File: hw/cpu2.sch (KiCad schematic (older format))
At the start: 0 parts

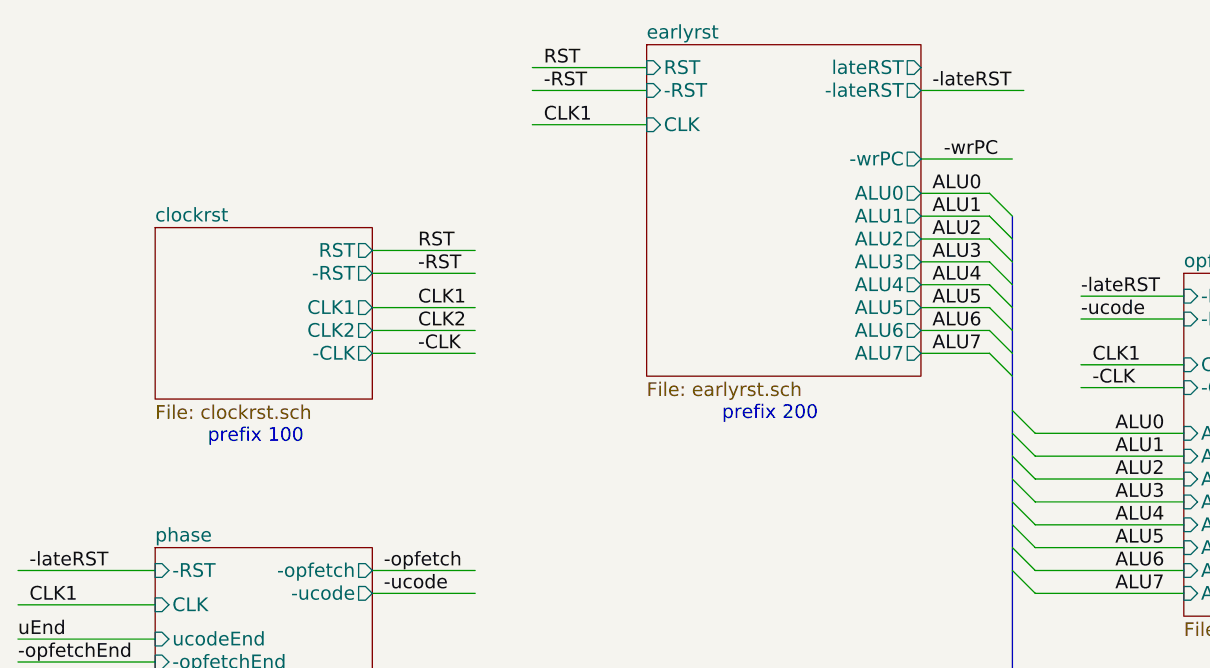
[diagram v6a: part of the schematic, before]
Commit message: buffer clock/reset signals in earlyrst module
This is the place that makes sense because the late
reset signal is the one that matters to the rest
of the circuit.
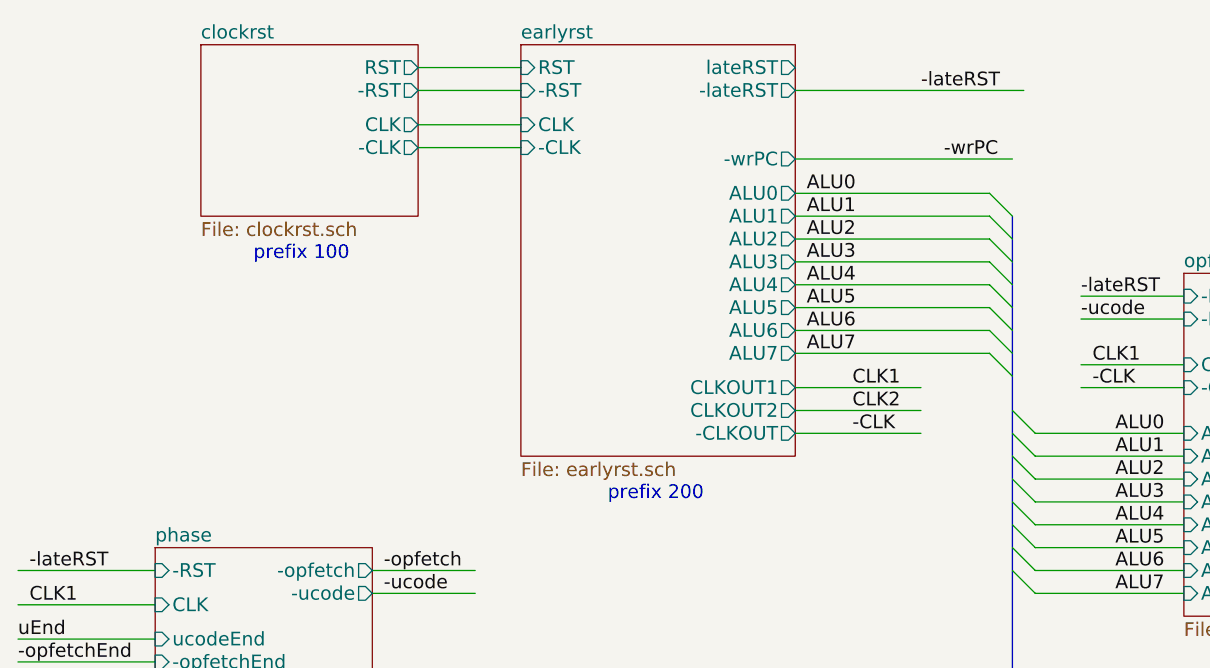
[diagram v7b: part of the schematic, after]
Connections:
- net labels removed: -RST, RST
- wire segments 233 -> 232
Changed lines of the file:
@@
 $EndSheet
 $Sheet
-S 3500 700  1200 1450
+S 2950 700  1200 1800
 U 592B9ACE
 F0 "earlyrst" 60
 F1 "earlyrst.sch" 60
-F2 "-RST" I L 3500 900 60
-F3 "RST" I L 3500 800 60
-F4 "CLK" I L 3500 1050 60
-F5 "-lateRST" O R 4700 900 60
-F6 "ALU0" O R 4700 1350 60
-F7 "ALU1" O R 4700 1450 60
-F8 "ALU2" O R 4700 1550 60
-F9 "ALU3" O R 4700 1650 60
-F10 "ALU4" O R 4700 1750 60
-F11 "ALU5" O R 4700 1850 60
-F12 "ALU6" O R 4700 1950 60
-F13 "ALU7" O R 4700 2050 60
-F14 "-wrPC" O R 4700 1200 60
-F15 "lateRST" O R 4700 800 60
+F2 "-RST" I L 2950 900 60
+F3 "RST" I L 2950 800 60
+F4 "CLK" I L 2950 1050 60
+F5 "-lateRST" O R 4150 900 60
+F6 "ALU0" O R 4150 1350 60
+F7 "ALU1" O R 4150 1450 60
+F8 "ALU2" O R 4150 1550 60
+F9 "ALU3" O R 4150 1650 60
+F10 "ALU4" O R 4150 1750 60
+F11 "ALU5" O R 4150 1850 60
+F12 "ALU6" O R 4150 1950 60
+F13 "ALU7" O R 4150 2050 60
+F14 "-wrPC" O R 4150 1200 60
+F15 "lateRST" O R 4150 800 60
+F16 "-CLK" I L 2950 1150 60
+F17 "CLKOUT1" O R 4150 2200 60
+F18 "CLKOUT2" O R 4150 2300 60
+F19 "-CLKOUT" O R 4150 2400 60
 $EndSheet
 $Sheet
@@
 $EndSheet
 $Sheet
-S 1350 1500 950  750
+S 1550 700  950  750
 U 59395B62
 F0 "clockrst" 60
 F1 "clockrst.sch" 60
-F2 "CLK1" O R 2300 1850 60
-F3 "CLK2" O R 2300 1950 60
-F4 "-CLK" O R 2300 2050 60
-F5 "RST" O R 2300 1600 60
-F6 "-RST" O R 2300 1700 60
+F2 "-CLK" O R 2500 1150 60
+F3 "RST" O R 2500 800 60
+F4 "-RST" O R 2500 900 60
+F5 "CLK" O R 2500 1050 60
 $EndSheet
-Text Notes 2000 2450 2    60   ~ 0
+Text Notes 2200 1650 2    60   ~ 0
 prefix 100
-Text Notes 4250 2350 2    60   ~ 0
+Text Notes 3750 2700 2    60   ~ 0
 prefix 200
-Text Label 4750 1350 0    60   ~ 0
+Text Label 4200 1350 0    60   ~ 0
 ALU0
-Text Label 4750 1450 0    60   ~ 0
+Text Label 4200 1450 0    60   ~ 0
 ALU1
-Text Label 4750 1550 0    60   ~ 0
+Text Label 4200 1550 0    60   ~ 0
 ALU2
-Text Label 4750 1650 0    60   ~ 0
+Text Label 4200 1650 0    60   ~ 0
 ALU3
-Text Label 4750 1750 0    60   ~ 0
+Text Label 4200 1750 0    60   ~ 0
 ALU4
-Text Label 4750 1850 0    60   ~ 0
+Text Label 4200 1850 0    60   ~ 0
 ALU5
-Text Label 4750 1950 0    60   ~ 0
+Text Label 4200 1950 0    60   ~ 0
 ALU6
-Text Label 4750 2050 0    60   ~ 0
+Text Label 4200 2050 0    60   ~ 0
 ALU7
 Entry Wire Line
@@
 	7550 11700 7650 11800
 Wire Wire Line
-	3000 800  3500 800
-Wire Wire Line
-	3000 900  3500 900
-Wire Wire Line
-	3000 1050 3500 1050
-Wire Wire Line
 	1350 3150 750  3150
 Wire Wire Line
 	1350 3000 750  3000
 Wire Wire Line
-	4700 900  5150 900
+	4150 900  5150 900
 Wire Wire Line
 	5400 1800 5850 1800
@@
 	5400 2100 5850 2100
 Wire Wire Line
-	4700 1350 5000 1350
-Wire Wire Line
-	4700 1450 5000 1450
-Wire Wire Line
-	4700 1550 5000 1550
-Wire Wire Line
-	4700 1650 5000 1650
-Wire Wire Line
-	4700 1750 5000 1750
-Wire Wire Line
-	4700 1850 5000 1850
-Wire Wire Line
-	4700 1950 5000 1950
-Wire Wire Line
-	4700 2050 5000 2050
+	4150 1350 5000 1350
+Wire Wire Line
+	4150 1450 5000 1450
+Wire Wire Line
+	4150 1550 5000 1550
+Wire Wire Line
+	4150 1650 5000 1650
+Wire Wire Line
+	4150 1750 5000 1750
+Wire Wire Line
+	4150 1850 5000 1850
+Wire Wire Line
+	4150 1950 5000 1950
+Wire Wire Line
+	4150 2050 5000 2050
 Wire Bus Line
 	5100 1450 5100 13100
@@
 	5850 4400 5200 4400
 Wire Wire Line
-	4700 1200 5100 1200
+	4150 1200 5100 1200
 Wire Wire Line
 	5250 4800 5850 4800
@@
 -opReadMem
 Wire Wire Line
-	2300 1600 2750 1600
-Wire Wire Line
-	2300 1700 2750 1700
-Wire Wire Line
-	2300 1850 2750 1850
-Wire Wire Line
-	2300 2050 2750 2050
-Text Label 2500 1600 0    60   ~ 0
-RST
-Text Label 2500 1700 0    60   ~ 0
--RST
-Text Label 2500 2050 0    60   ~ 0
--CLK
-Text Label 4750 900  0    60   ~ 0
+	2500 800  2950 800
+Wire Wire Line
+	2500 900  2950 900
+Wire Wire Line
+	2500 1050 2950 1050
+Wire Wire Line
+	2500 1150 2950 1150
+Text Label 4700 900  0    60   ~ 0
 -lateRST
 Text Label 5400 1900 0    60   ~ 0
@@
 Text Label 7800 1800 0    60   ~ 0
 -opfetch
-Text Label 3050 800  0    60   ~ 0
-RST
-Text Label 3050 900  0    60   ~ 0
--RST
 Wire Wire Line
 	10150 1700 10700 1700
@@
 Text Label 7850 10100 0    60   ~ 0
 -uAluOut
-Wire Wire Line
-	2300 1950 2750 1950
-Text Label 2500 1850 0    60   ~ 0
-CLK1
-Text Label 2500 1950 0    60   ~ 0
-CLK2
 Text Label 800  3150 0    60   ~ 0
-CLK1
-Text Label 3050 1050 0    60   ~ 0
 CLK1
 Text Label 7800 2000 0    60   ~ 0
@@
 Text Label 7950 3850 0    60   ~ 0
 -opfetch
+Wire Wire Line
+	4150 2200 4700 2200
+Wire Wire Line
+	4150 2300 4700 2300
+Wire Wire Line
+	4150 2400 4700 2400
+Text Label 4400 2200 0    60   ~ 0
+CLK1
+Text Label 4400 2300 0    60   ~ 0
+CLK2
+Text Label 4400 2400 0    60   ~ 0
+-CLK
 $EndSCHEMATC

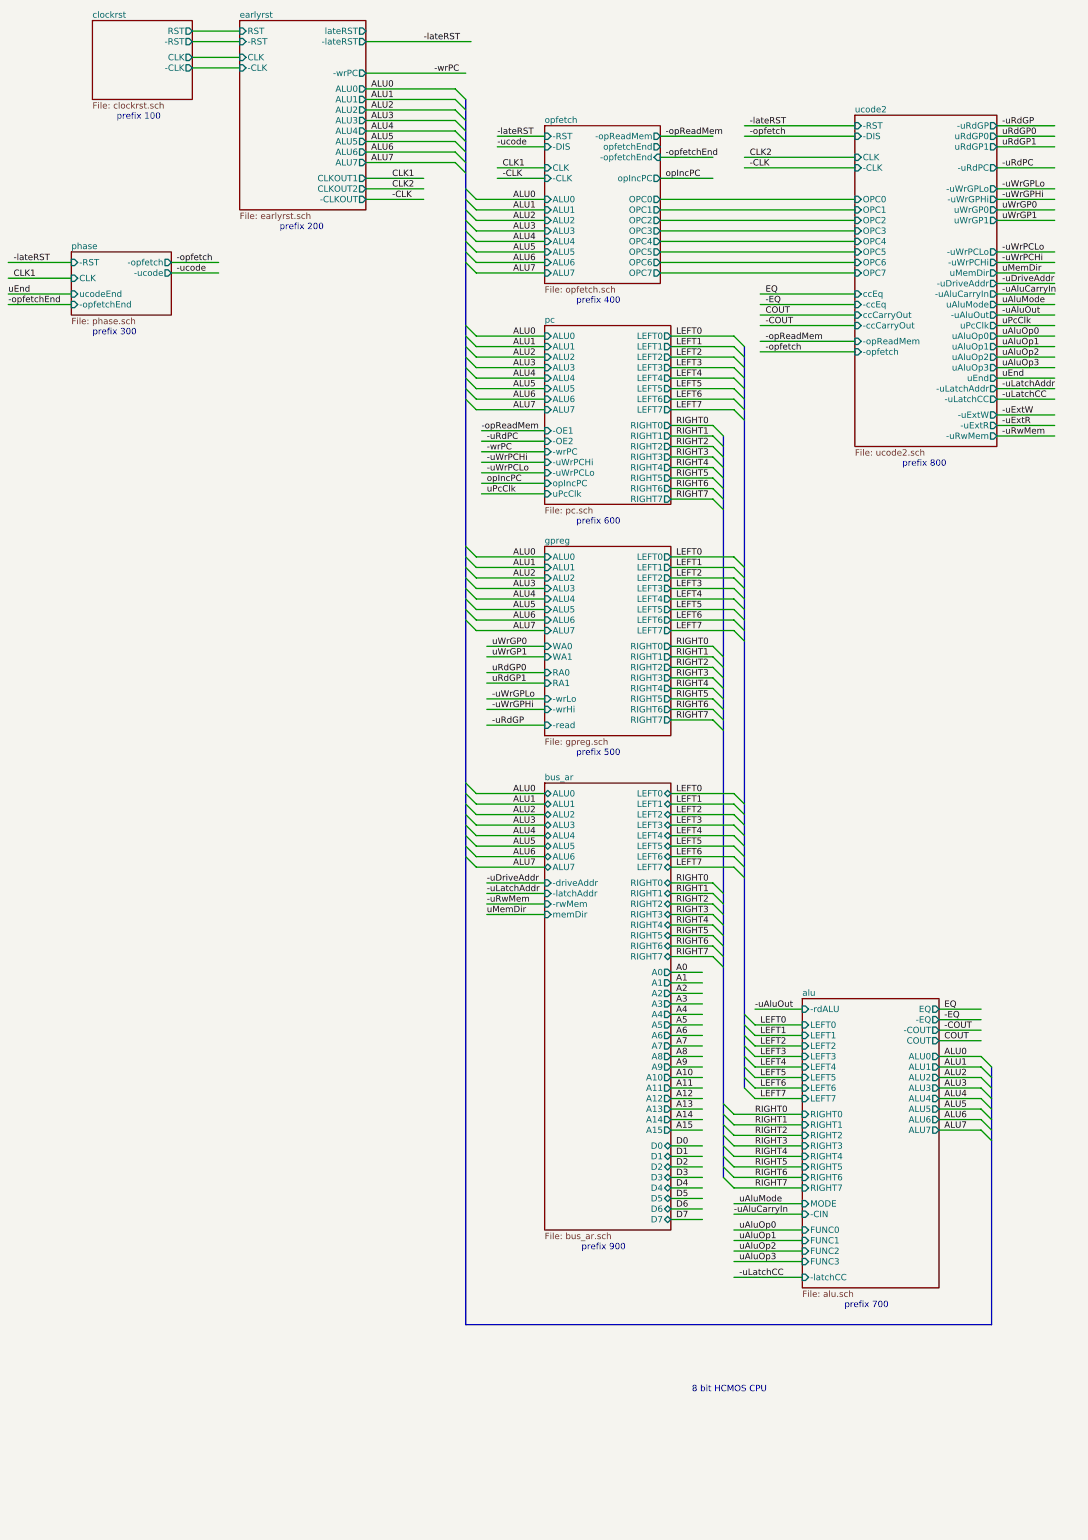
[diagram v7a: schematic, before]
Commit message: allow ALU output to be latched
We can do this with essentially no increase in
complexity, using a '573 latch rather than a '541
buffer for the ALU output.  I'm guessing this
might be useful for some instructions (to hold the
ALU output constant when its inputs might be
changing.)
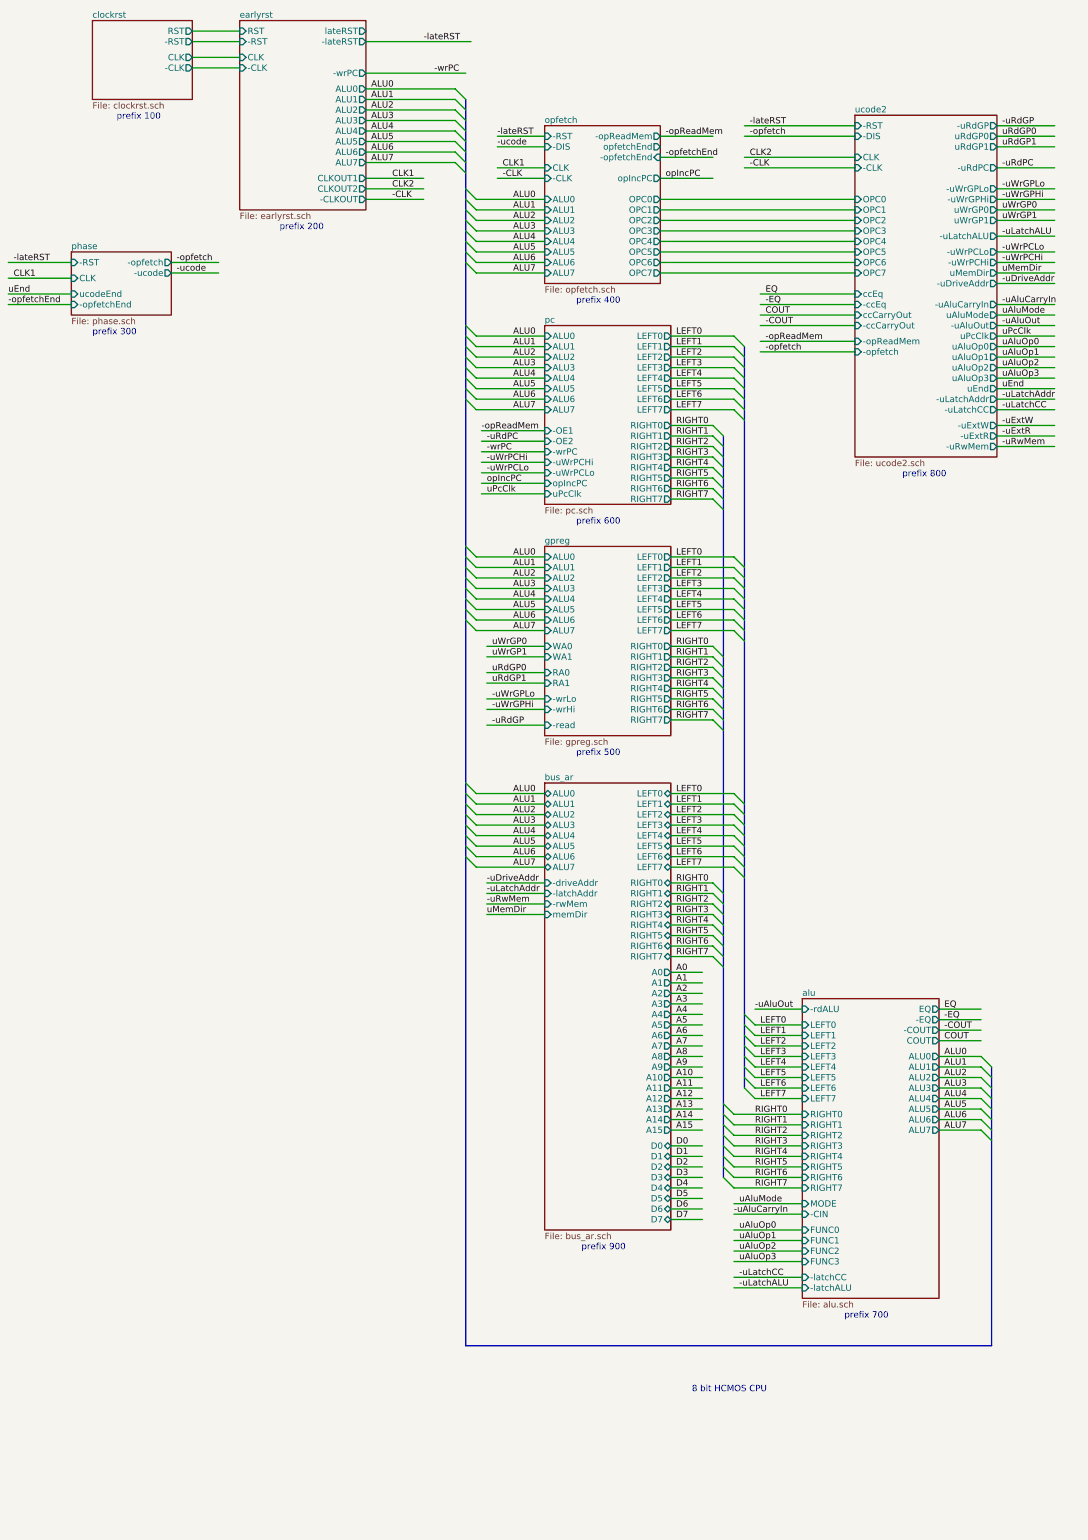
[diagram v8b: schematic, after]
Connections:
- net labels added: -uLatchALU
- wire segments 232 -> 234
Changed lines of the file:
@@
 Text Notes 6150 3400 0    60   ~ 0
 prefix 400
-Text Notes 9250 4950 0    60   ~ 0
+Text Notes 9250 5050 0    60   ~ 0
 prefix 800
 Text Notes 6150 5500 0    60   ~ 0
@@
 Text Label 5300 5200 0    60   ~ 0
 uPcClk
-Text Label 10200 3600 0    60   ~ 0
+Text Label 10200 3700 0    60   ~ 0
 uPcClk
-Text Label 10200 4100 0    60   ~ 0
+Text Label 10200 4200 0    60   ~ 0
 uEnd
 Text Label 750  3300 0    60   ~ 0
@@
 8 bit HCMOS CPU
 $Sheet
-S 8300 10000 1300 2750
+S 8300 10000 1300 2850
 U 5947DA38
 F0 "alu" 60
@@
 F36 "COUT" O R 9600 10400 60
 F37 "-latchCC" I L 8300 12650 60
+F38 "-latchALU" I L 8300 12750 60
 $EndSheet
-Text Notes 8700 12950 0    60   ~ 0
+Text Notes 8700 13050 0    60   ~ 0
 prefix 700
 Text Label 7100 3700 0    60   ~ 0
@@
 	4150 2050 5000 2050
 Wire Bus Line
-	5100 1450 5100 13100
+	5100 1450 5100 13300
 Wire Wire Line
 	5850 2400 5200 2400
@@
 	6950 3100 8800 3100
 Wire Wire Line
-	10150 3600 10700 3600
-Wire Wire Line
-	10150 4100 10700 4100
+	10150 3700 10700 3700
+Wire Wire Line
+	10150 4200 10700 4200
 Wire Wire Line
 	1350 3300 750  3300
@@
 	8300 11800 7650 11800
 Wire Bus Line
-	10100 13100 5100 13100
+	10100 13300 5100 13300
 Wire Bus Line
-	10100 10650 10100 13100
+	10100 10650 10100 13300
 Wire Wire Line
 	9600 10550 10000 10550
@@
 	10000 11250 10100 11350
 $Sheet
-S 8800 1600 1350 3150
+S 8800 1600 1350 3250
 U 594ECB9B
 F0 "ucode2" 60
@@
 F22 "-uWrPCLo" O R 10150 2900 60
 F23 "-uWrPCHi" O R 10150 3000 60
-F24 "-uAluCarryIn" O R 10150 3300 60
-F25 "uAluMode" O R 10150 3400 60
-F26 "uAluOp0" O R 10150 3700 60
-F27 "uAluOp1" O R 10150 3800 60
-F28 "uAluOp2" O R 10150 3900 60
-F29 "uAluOp3" O R 10150 4000 60
-F30 "-uAluOut" O R 10150 3500 60
+F24 "-uAluCarryIn" O R 10150 3400 60
+F25 "uAluMode" O R 10150 3500 60
+F26 "uAluOp0" O R 10150 3800 60
+F27 "uAluOp1" O R 10150 3900 60
+F28 "uAluOp2" O R 10150 4000 60
+F29 "uAluOp3" O R 10150 4100 60
+F30 "-uAluOut" O R 10150 3600 60
 F31 "ccEq" I L 8800 3300 60
 F32 "-ccEq" I L 8800 3400 60
@@
 F34 "-ccCarryOut" I L 8800 3600 60
 F35 "-uDriveAddr" O R 10150 3200 60
-F36 "uPcClk" O R 10150 3600 60
-F37 "uEnd" O R 10150 4100 60
+F36 "uPcClk" O R 10150 3700 60
+F37 "uEnd" O R 10150 4200 60
 F38 "uMemDir" O R 10150 3100 60
-F39 "-uLatchAddr" O R 10150 4200 60
-F40 "-uExtW" O R 10150 4450 60
-F41 "-uExtR" O R 10150 4550 60
-F42 "-uLatchCC" O R 10150 4300 60
-F43 "-uRwMem" O R 10150 4650 60
+F39 "-uLatchAddr" O R 10150 4300 60
+F40 "-uExtW" O R 10150 4550 60
+F41 "-uExtR" O R 10150 4650 60
+F42 "-uLatchCC" O R 10150 4400 60
+F43 "-uRwMem" O R 10150 4750 60
 F44 "-opReadMem" I L 8800 3750 60
 F45 "-opfetch" I L 8800 3850 60
+F46 "-uLatchALU" O R 10150 2750 60
 $EndSheet
 Wire Wire Line
@@
 	10150 3200 10700 3200
 Wire Wire Line
-	10150 3300 10700 3300
-Wire Wire Line
 	10150 3400 10700 3400
 Wire Wire Line
 	10150 3500 10700 3500
 Wire Wire Line
-	10150 3700 10700 3700
+	10150 3600 10700 3600
 Wire Wire Line
 	10150 3800 10700 3800
@@
 Wire Wire Line
 	10150 4000 10700 4000
+Wire Wire Line
+	10150 4100 10700 4100
 Text Label 10200 1700 0    60   ~ 0
 -uRdGP
@@
 Text Label 10200 3200 0    60   ~ 0
 -uDriveAddr
-Text Label 10200 3300 0    60   ~ 0
+Text Label 10200 3400 0    60   ~ 0
 -uAluCarryIn
-Text Label 10200 3400 0    60   ~ 0
+Text Label 10200 3500 0    60   ~ 0
 uAluMode
-Text Label 10200 3500 0    60   ~ 0
+Text Label 10200 3600 0    60   ~ 0
 -uAluOut
-Text Label 10200 3700 0    60   ~ 0
+Text Label 10200 3800 0    60   ~ 0
 uAluOp0
-Text Label 10200 3800 0    60   ~ 0
+Text Label 10200 3900 0    60   ~ 0
 uAluOp1
-Text Label 10200 3900 0    60   ~ 0
+Text Label 10200 4000 0    60   ~ 0
 uAluOp2
-Text Label 10200 4000 0    60   ~ 0
+Text Label 10200 4100 0    60   ~ 0
 uAluOp3
 Wire Wire Line
@@
 $EndSheet
 Wire Wire Line
-	10150 4650 10700 4650
-Text Label 10200 4650 0    60   ~ 0
+	10150 4750 10700 4750
+Text Label 10200 4750 0    60   ~ 0
 -uRwMem
 Wire Wire Line
@@
 -uLatchAddr
 Wire Wire Line
-	10150 4200 10700 4200
-Text Label 10200 4200 0    60   ~ 0
--uLatchAddr
-Wire Wire Line
-	10150 4450 10700 4450
-Wire Wire Line
-	10150 4550 10700 4550
-Text Label 10200 4450 0    60   ~ 0
--uExtW
-Text Label 10200 4550 0    60   ~ 0
--uExtR
-Wire Wire Line
 	10150 4300 10700 4300
 Text Label 10200 4300 0    60   ~ 0
+-uLatchAddr
+Wire Wire Line
+	10150 4550 10700 4550
+Wire Wire Line
+	10150 4650 10700 4650
+Text Label 10200 4550 0    60   ~ 0
+-uExtW
+Text Label 10200 4650 0    60   ~ 0
+-uExtR
+Wire Wire Line
+	10150 4400 10700 4400
+Text Label 10200 4400 0    60   ~ 0
 -uLatchCC
 Wire Wire Line
@@
 Text Label 4400 2400 0    60   ~ 0
 -CLK
+Wire Wire Line
+	10150 2750 10700 2750
+Text Label 10200 2750 0    60   ~ 0
+-uLatchALU
+Wire Wire Line
+	8300 12750 7650 12750
+Text Label 7700 12750 0    60   ~ 0
+-uLatchALU
 $EndSCHEMATC
